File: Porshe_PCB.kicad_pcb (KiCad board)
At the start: 2 copper layers, 56.6 x 66.5 mm, 36 parts, among them IC1 RASPBERRY_PI_PICO_W, J1 Conn_01x04_Socket, J10 Conn_01x03_Socket, J11 Conn_01x04_Socket, J12 Conn_01x01_Pin, J2 SM04B-SRSS-TB_LF__SN_, J3 Conn_01x04_Socket, J4 S2B-PH-SM4-TB_LF__SN_, J5 Screw_Terminal_01x03, J6 Conn_01x01_Pin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

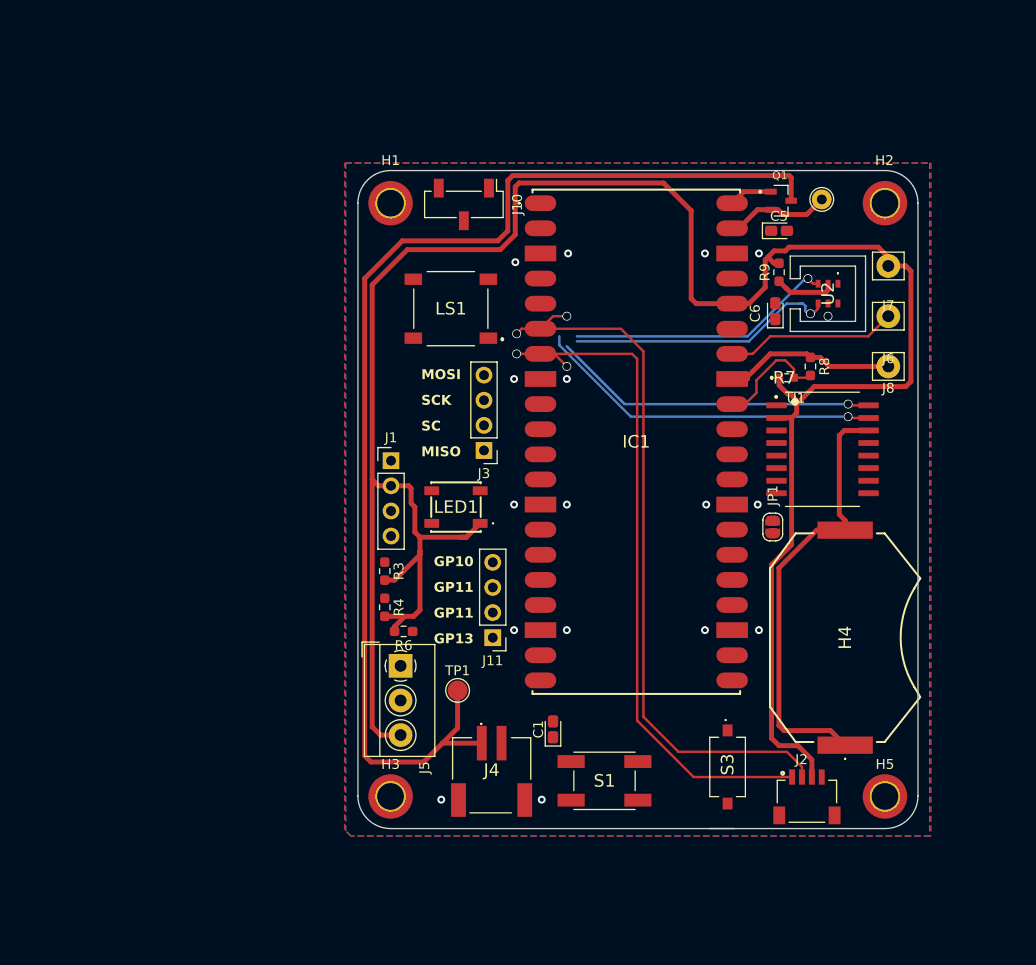
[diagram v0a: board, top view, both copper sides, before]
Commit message: 코인베터리 접지추가
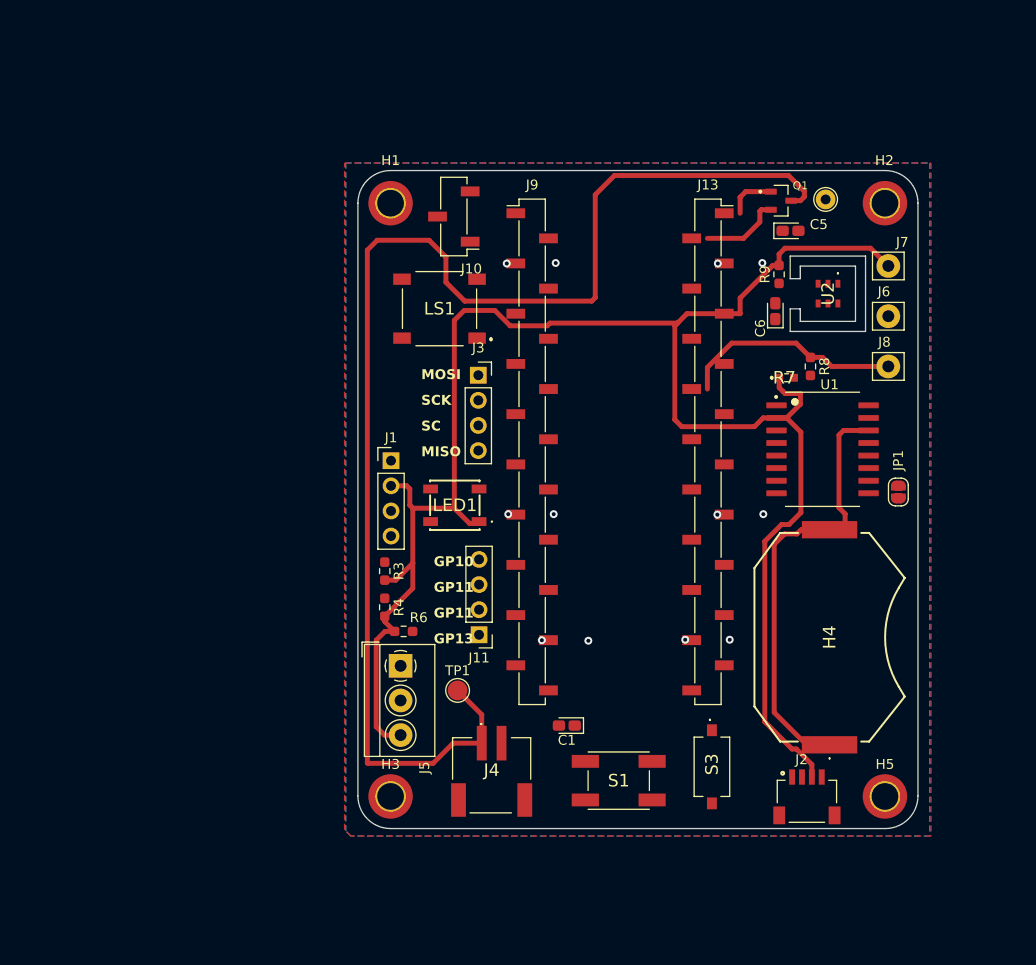
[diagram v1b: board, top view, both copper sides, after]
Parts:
- removed IC1: RASPBERRY_PI_PICO_W, PICO_W:RASPBERRYPIPICOW
- added J13: Conn_01x20_Socket, Connector_PinSocket_2.54mm:PinSocket_1x20_P2.54mm_Vertical_SMD_Pin1Right, F.Cu at (149.4, 88.6)
- added J9: Conn_01x20_Socket, Connector_PinSocket_2.54mm:PinSocket_1x20_P2.54mm_Vertical_SMD_Pin1Left, F.Cu at (131.6, 88.6)
- J3: footprint Connector_PinHeader_2.54mm:PinHeader_1x04_P2.54mm_Vertical -> Connector_PinSocket_2.54mm:PinSocket_1x04_P2.54mm_Vertical
- moved JP1 13.2 mm to (168.7, 92.7)
- moved J3 7.63 mm to (126.2, 80.9), turned to 0 degrees
- moved J10 1.59 mm to (123.7, 64.8), turned to 180 degrees
- moved S3 1.58 mm to (149.8, 120.5)
- moved H4 1.57 mm to (161.7, 107.4)
- moved C1 1.45 mm to (135.1, 116.3), turned to 180 degrees
- moved S1 1.44 mm to (140.4, 121.9)
- moved J11 1.42 mm to (126.2, 107.2)
- moved C5 1.16 mm to (157.8, 66.3)
- moved LS1 1.14 mm to (122.3, 74.2)
- moved J12 0.39 mm to (161.3, 63.1)
- moved LED1 0.22 mm to (123.8, 94.0)
- moved R9 0.22 mm to (156.6, 70.7)
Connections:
- net Net-(J4-Pad1) renamed /BATT(+)
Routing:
- net /SDA: track 135.9 -> 0.00 mm, vias 4 -> 0
- net /SCL: track 130.2 -> 0.00 mm, vias 4 -> 0
- net /3V3: track 232.8 -> 181.7 mm
- net /ADC2: track 17.4 -> 0.00 mm
- net /BATT(+): track 120.0 -> 133.4 mm
- net /Light: track 11.8 -> 0.00 mm
- net Net-(U2-VDD): track 6.14 -> 0.00 mm
- net GNDA: track 19.8 -> 22.5 mm
- net /VSYS: track 10.7 -> 8.28 mm
- net Net-(U1-VBAT): track 44.7 -> 46.4 mm
- net /VBUS: track 4.41 -> 4.97 mm
- net GND: vias 17 -> 12
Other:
- outline, holes or cut-outs redrawn

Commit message: 오토라우팅완료
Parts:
- J6, J7, J8: footprint Connector_Pin:Pin_D1.2mm_L10.2mm_W2.9mm_FlatFork -> Connector_Pin:Pin_D1.3mm_L11.0mm
- TP1: footprint TestPoint:TestPoint_Pad_D2.0mm -> TestPoint:TestPoint_Pad_D1.0mm
- moved G*** 70.0 mm to (137.2, 91.9), turned to 90 degrees
- moved Q1 58.4 mm to (126.2, 113.0)
- moved JP1 5.84 mm to (168.7, 86.9)
- moved TP1 2.79 mm to (125.2, 110.2)
- moved R7 2.22 mm to (155.4, 80.0)
- moved C5 1.28 mm to (159.0, 66.0)
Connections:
- net /BATT(+) renamed /VBAT(+)
- net Net-(U1-VBAT) renamed /BAK_VBAT
- J7 pad 1: /3V3 -> GNDA
- J8 pad 1: GNDA -> /3V3
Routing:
- net /SDA: track 0.00 -> 149.5 mm, vias 0 -> 3
- net /SCL: track 0.00 -> 126.8 mm, vias 0 -> 3
- net /VBAT(+): track 133.4 -> 10.3 mm
- net /VSYS: track 8.28 -> 101.9 mm, vias 0 -> 2
- net /VBUS: track 4.97 -> 88.8 mm, vias 0 -> 2
- net /SPI_SC: track 0.00 -> 55.9 mm, vias 0 -> 1
- net /DI: track 0.00 -> 43.6 mm
- net /SPI0_MISO: track 0.00 -> 43.5 mm, vias 0 -> 1
- net /SPI0_SCK: track 0.00 -> 34.8 mm
- net GNDA: track 22.5 -> 53.3 mm
- net /RUN: track 0.00 -> 29.8 mm
- net /RTC_RST: track 0.00 -> 28.8 mm
- net /SPI0_MOSI: track 0.00 -> 28.3 mm
- net Net-(U2-VDD): track 0.00 -> 23.8 mm, vias 0 -> 2
- net /3V3: track 181.7 -> 204.7 mm, vias 0 -> 5
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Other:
- board text added: "3V"
- board text added: "3V3"
- board text added: "ADC"
- board text added: "BATT"
- board text added: "Button"
- board text added: "COIN BAT"
- board text added: "DI"
- board text added: "GND"
- board text added: "GNDA"
- board text added: "I2C"
- board text added: "Light"
- board text added: "RTC"
- board text added: "RX"
- board text added: "Reset"
- board text added: "SCL"
- board text added: "SDA"
- board text added: "TX"
- board text added: "Temp / Humi"

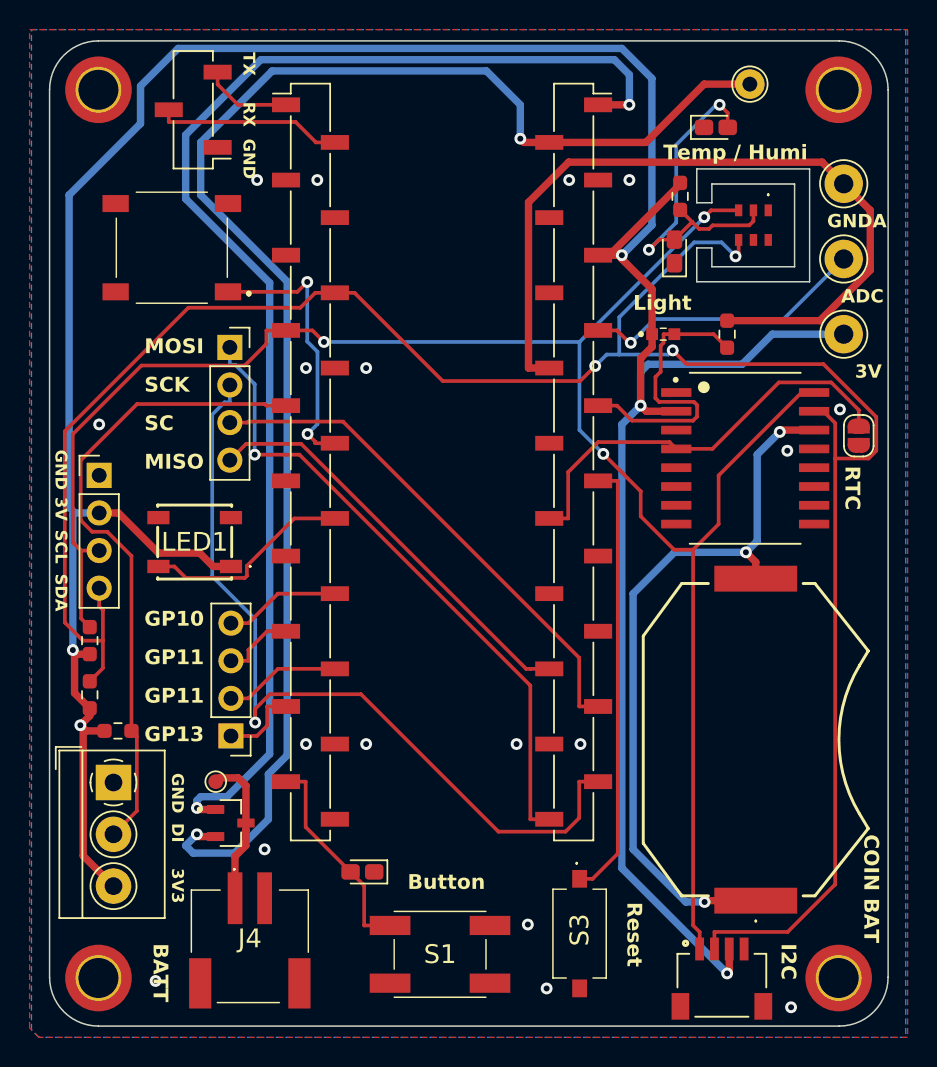
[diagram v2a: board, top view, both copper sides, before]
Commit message: BOM확인후 부품 배치완료
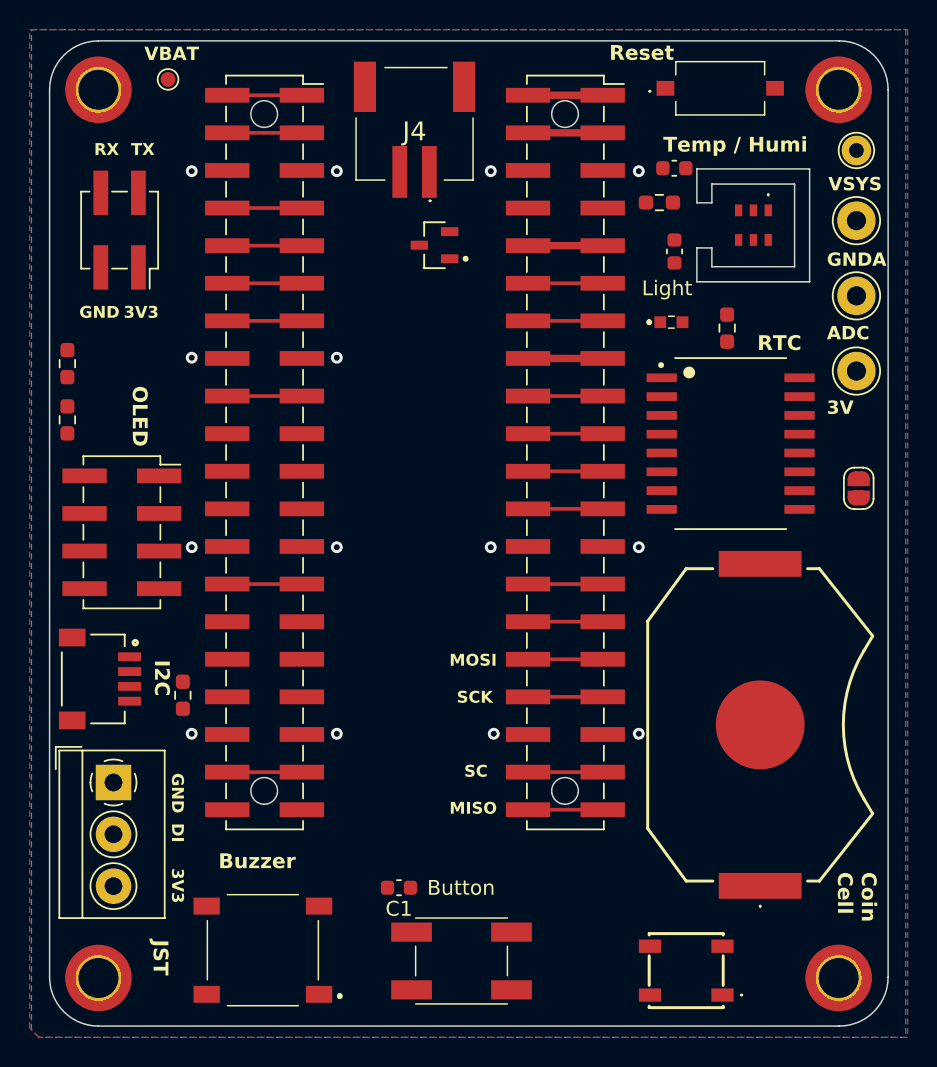
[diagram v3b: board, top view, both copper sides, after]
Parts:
- removed J1, J11: Conn_01x04_Socket, Connector_PinHeader_2.54mm:PinHeader_1x04_P2.54mm_Vertical
- removed J10: Conn_01x03_Socket, Connector_PinSocket_2.54mm:PinSocket_1x03_P2.54mm_Vertical_SMD_Pin1Left
- removed J13: Conn_01x20_Socket, Connector_PinSocket_2.54mm:PinSocket_1x20_P2.54mm_Vertical_SMD_Pin1Right
- added J14: Conn_02x20_Odd_Even, Connector_PinSocket_2.54mm:PinSocket_2x20_P2.54mm_Vertical_SMD, F.Cu at (148.8, 88.0)
- added J16: Conn_02x20_Odd_Even, Connector_PinSocket_2.54mm:PinSocket_2x20_P2.54mm_Vertical_SMD, F.Cu at (128.5, 88.0)
- added P1: ~, ConCell_GND:CR2032_GND, F.Cu at (162.0, 106.4)
- C1: footprint Capacitor_Tantalum_SMD:CP_EIA-1608-08_AVX-J_Pad1.25x1.05mm_HandSolder -> Capacitor_SMD:C_0603_1608Metric
- C5, C6: footprint Capacitor_Tantalum_SMD:CP_EIA-1608-10_AVX-L_Pad1.25x1.05mm_HandSolder -> Capacitor_SMD:C_0603_1608Metric
- J3: value Conn_01x04_Socket -> Conn_02x02_Odd_Even; footprint Connector_PinSocket_2.54mm:PinSocket_1x04_P2.54mm_Vertical -> Connector_PinSocket_2.54mm:PinSocket_2x02_P2.54mm_Vertical_SMD
- J9: value Conn_01x20_Socket -> Conn_02x04_Odd_Even; footprint Connector_PinSocket_2.54mm:PinSocket_1x20_P2.54mm_Vertical_SMD_Pin1Left -> Connector_PinSocket_2.54mm:PinSocket_2x04_P2.54mm_Vertical_SMD
- moved S3 57.9 mm to (159.3, 63.4), turned to 0 degrees
- moved J4 56.7 mm to (138.7, 65.8), turned to 0 degrees
- moved LS1 47.8 mm to (128.4, 121.6)
- moved TP1 47.5 mm to (122.0, 62.8)
- moved LED1 44.0 mm to (157.0, 123.0)
- moved J2 44.0 mm to (119.4, 103.3), turned to -90 degrees
- moved Q1 41.4 mm to (140.0, 74.0), turned to 180 degrees
- moved R4 22.4 mm to (115.2, 82.0)
- moved R3 15.0 mm to (115.2, 85.8)
- moved J9 13.6 mm to (118.9, 93.4)
- moved J3 10.9 mm to (118.7, 73.0), turned to -90 degrees
- moved J12 8.48 mm to (168.5, 67.6)
- moved R6 5.00 mm to (123.0, 104.4), turned to 90 degrees
- moved C5 3.93 mm to (156.2, 68.8)
- moved JP1 3.56 mm to (168.7, 90.4)
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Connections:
- J3 pad 1: /SPI0_MISO -> /3V3
- J3 pad 2: /SPI_SC -> /UART0_TX
- J3 pad 3: /SPI0_SCK -> GND
- J3 pad 4: /SPI0_MOSI -> /UART0_RX
- J9 pad 1: /UART0_TX -> /3V3
- J9 pad 2: /UART0_RX -> /3V3
- J9 pad 4: unconnected-(J9-Pin_4-Pad4) -> GND
- J9 pad 5: unconnected-(J9-Pin_5-Pad5) -> /SCL
- J9 pad 6: /SDA -> /SCL
- J9 pad 7: /SCL -> /SDA
- J9 pad 8: GND -> /SDA
- R3 pad 1: /SCL -> /SDA
- R4 pad 1: /SDA -> /SCL
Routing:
- net /3V3: track 204.7 -> 5.04 mm, vias 5 -> 0
- net /SDA: track 149.5 -> 5.04 mm, vias 3 -> 0
- net /SCL: track 126.8 -> 5.04 mm, vias 3 -> 0
- net /VSYS: track 101.9 -> 5.04 mm, vias 2 -> 0
- net /VBUS: track 88.8 -> 5.04 mm, vias 2 -> 0
- net /SPI_SC: track 55.9 -> 5.04 mm, vias 1 -> 0
- net /BAK_VBAT: track 49.3 -> 0.00 mm, vias 3 -> 0
- net GNDA: track 53.3 -> 5.04 mm
- net /DI: track 43.6 -> 5.04 mm
- net /SPI0_MISO: track 43.5 -> 5.04 mm, vias 1 -> 0
- net /SPI0_SCK: track 34.8 -> 5.04 mm
- net /RUN: track 29.8 -> 5.04 mm
- net Net-(U2-VDD): track 23.8 -> 0.00 mm, vias 2 -> 0
- net /RTC_RST: track 28.8 -> 5.04 mm
- net /SPI0_MOSI: track 28.3 -> 5.04 mm
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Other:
- outline, holes or cut-outs redrawn
- board text added: "Buzzer"
- board text added: "Coin Cell"
- board text added: "JST"
- board text added: "OLED"
- board text added: "VBAT"
- board text added: "VSYS"
- board text removed: "BATT"
- board text removed: "COIN BAT"
- board text removed: "GP10"
- board text removed: "GP11"
- board text removed: "GP13"
- board text removed: "SCL"
- board text removed: "SDA"
- board text removed: "SmartFarm Ver0_1"
- board text removed: "https://github.com/microschool-kr/Microschool-DataPi-SmartFarm"

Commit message: 회로도 완성
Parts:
- removed C5: 10uF/10V(10%), Capacitor_SMD:C_0603_1608Metric
- removed C6: 0.1uF/10V(10%), Capacitor_SMD:C_0603_1608Metric
- removed H5: MountingHole_Pad, MountingHole:MountingHole_2.7mm_M2.5_ISO7380_Pad_TopOnly
- removed U2: AHT20, AHT20:AHT20
- added C2: 1uF/50V(10%), Capacitor_SMD:C_0603_1608Metric, F.Cu at (153.2, 129.5)
- added IC2: BH1750FVI-TR, BH1750:WSOF6, F.Cu at (154.8, 127.5)
- added J1: TF-115, TF-115:TF115, F.Cu at (156.5, 109.2)
- added J10: Conn_01x01_Pin, TestPoint:TestPoint_THTPad_D2.0mm_Drill1.0mm, F.Cu at (149.6, 121.5)
- added J11: Conn_01x01_Pin, TestPoint:TestPoint_THTPad_D2.0mm_Drill1.0mm, F.Cu at (149.6, 125.7)
- added JP2: Jumper_2_Open, Jumper:SolderJumper-2_P1.3mm_Open_RoundedPad1.0x1.5mm, F.Cu at (153.0, 120.7)
- added JP3: Jumper_2_Bridged, Jumper:SolderJumper-2_P1.3mm_Bridged_RoundedPad1.0x1.5mm, F.Cu at (126.0, 81.9)
- added R1: 4.7k, Resistor_SMD:R_0603_1608Metric_Pad0.98x0.95mm_HandSolder, F.Cu at (141.3, 101.2)
- added R2: 4.7k, Resistor_SMD:R_0603_1608Metric_Pad0.98x0.95mm_HandSolder, F.Cu at (145.0, 100.7)
- added R5: 1k, Resistor_SMD:R_0603_1608Metric_Pad0.98x0.95mm_HandSolder, F.Cu at (156.6, 122.2)
- added TP2: TestPoint, TestPoint:TestPoint_Pad_D1.0mm, F.Cu at (140.8, 115.5)
- added TP3: TestPoint, TestPoint:TestPoint_Pad_D1.0mm, F.Cu at (143.8, 115.5)
- J5: value Screw_Terminal_01x03 -> Conn_01x01_Pin; footprint TerminalBlock_4Ucon:TerminalBlock_4Ucon_1x03_P3.50mm_Horizontal -> TestPoint:TestPoint_THTPad_D2.0mm_Drill1.0mm
- R7: value ALS-PT19-315C_L177_TR8 -> 10k; footprint ALS-PT19-315C:ALSPT19315CL177TR8 -> Resistor_SMD:R_0603_1608Metric_Pad0.98x0.95mm_HandSolder
- R8: value 10K(5%) -> 10k
- R9: value 220 -> 10k
- moved H2 86.0 mm to (104.0, 121.7)
- moved J12 81.0 mm to (94.6, 100.7)
- moved S3 72.6 mm to (100.0, 105.3), turned to 180 degrees
- moved JP1 62.0 mm to (112.2, 116.1), turned to 180 degrees
- moved U1 48.4 mm to (115.4, 106.3)
- moved J2 47.3 mm to (160.2, 79.4), turned to 90 degrees
- moved R7 45.5 mm to (156.6, 124.7)
- moved H3 43.8 mm to (161.0, 121.7)
- moved J3 42.9 mm to (103.0, 112.9), turned to 0 degrees
- moved J5 37.2 mm to (149.6, 130.3)
- moved R8 36.3 mm to (124.1, 86.4), turned to 90 degrees
- moved H4 35.9 mm to (132.6, 126.9), turned to 0 degrees
- moved P1 35.9 mm to (132.6, 126.9)
- moved R6 35.5 mm to (152.9, 123.5), turned to 180 degrees
- moved J4 34.0 mm to (110.2, 84.5), turned to 90 degrees
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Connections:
- net /GP10 renamed /SPI1_SCK
- net /GP12 renamed /Light_RST
- net /SPI0_SCK renamed Net-(J14-Pin_33)
- J14 pad 17: /Light -> /BAT_DIV
- J14 pad 18: /Light -> /BAT_DIV
- J14 pad 31: /SPI0_MOSI -> Net-(J14-Pin_31)
- J14 pad 32: /SPI0_MOSI -> Net-(J14-Pin_31)
- J14 pad 37: /SPI_SC -> Net-(J14-Pin_37)
- J14 pad 38: /SPI_SC -> Net-(J14-Pin_37)
- J14 pad 39: /SPI0_MISO -> Net-(J14-Pin_39)
- J14 pad 40: /SPI0_MISO -> Net-(J14-Pin_39)
- J14 pad 7: unconnected-(J14-Pin_7-Pad7) -> Net-(J14-Pin_7)
- J14 pad 8: unconnected-(J14-Pin_8-Pad8) -> Net-(J14-Pin_7)
- J16 pad 21: unconnected-(J16-Pin_21-Pad21) -> /SPI0_MISO
- J16 pad 22: unconnected-(J16-Pin_22-Pad22) -> /SPI0_MISO
- J16 pad 23: /LED -> /SPI_SC
- J16 pad 24: /LED -> /SPI_SC
- J16 pad 29: /GP11 -> /SPI0_MOSI
- J16 pad 30: /GP11 -> /SPI0_MOSI
- J16 pad 33: /GP13 -> /LED
- J16 pad 34: /GP13 -> /LED
- J5 pad 1: GND -> /3V3
- R7 pad 1: /3V3 -> GND
- R7 pad 2: /Light -> Net-(IC2-ADDR)
- R8 pad 1: GNDA -> Net-(JP3-A)
- R8 pad 2: /Light -> /VBAT(+)
- R9 pad 1: Net-(U2-VDD) -> Net-(JP3-A)
- R9 pad 2: /3V3 -> /VBAT(+)
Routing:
- net Net-(J14-Pin_33): track 5.04 -> 0.00 mm
- net Net-(J14-Pin_29): track 5.04 -> 0.00 mm
- net Net-(J14-Pin_27): track 5.04 -> 0.00 mm
- net Net-(J14-Pin_19): track 5.04 -> 0.00 mm
- net Net-(J14-Pin_11): track 5.04 -> 0.00 mm
- net GNDA: track 5.04 -> 0.00 mm
- net /VSYS: track 5.04 -> 0.00 mm
- net /VBUS: track 5.04 -> 0.00 mm
- net /SPI_SC: track 5.04 -> 0.00 mm
- net /SPI0_MOSI: track 5.04 -> 0.00 mm
- net /SPI0_MISO: track 5.04 -> 0.00 mm
- net /RUN: track 5.04 -> 0.00 mm
- net /RTC_RST: track 5.04 -> 0.00 mm
- net /Light: track 5.04 -> 0.00 mm
- net /ADC2: track 5.04 -> 0.00 mm
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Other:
- board size 56.6 x 66.5 mm -> 80 x 80 mm
- board text removed: "MISO"
- board text removed: "MOSI"
- board text removed: "SC"
- board text removed: "SCK"
- board text removed: "Temp / Humi"
